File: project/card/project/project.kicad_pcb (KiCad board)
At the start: 2 copper layers, 29 parts, among them J1 USB_OTG, J2 Conn_01x06_Male, J3 Conn_01x02_Male, J5 Conn_Coaxial, J6 Conn_01x07_Female, J7 Conn_01x05_Female, SW1 SW_Push, SW2 SW_Push, U1 LM1117ADJ, U2 CMWX1ZZABZ-078

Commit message: layout etc
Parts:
- added C14: _, Capacitor_SMD:C_0805_2012Metric_Pad1.15x1.40mm_HandSolder, F.Cu at (94.8, 62.8)
- added C16: _, Capacitor_SMD:C_0805_2012Metric_Pad1.15x1.40mm_HandSolder, F.Cu at (95.7, 59.6)
- added D2: LED, LED_SMD:LED_0805_2012Metric_Pad1.15x1.40mm_HandSolder, F.Cu at (62.6, 72.5)
- added R4: 660, Resistor_SMD:R_0805_2012Metric_Pad1.15x1.40mm_HandSolder, F.Cu at (59.5, 72.5)
- added R5: 220, Resistor_SMD:R_0805_2012Metric_Pad1.15x1.40mm_HandSolder, F.Cu at (91.2, 52.5)
- C13: footprint Capacitor_SMD:CP_Elec_5x4.5 -> Capacitor_SMD:C_0805_2012Metric_Pad1.15x1.40mm_HandSolder
- J2: footprint Connector_Molex:Molex_KK-254_AE-6410-06A_1x06_P2.54mm_Vertical -> Connector_PinHeader_2.54mm:PinHeader_1x06_P2.54mm_Vertical
- J3: footprint Connector_Molex:Molex_KK-254_AE-6410-02A_1x02_P2.54mm_Vertical -> Connector_PinHeader_2.54mm:PinHeader_1x02_P2.54mm_Vertical
- J6: footprint Connector_Molex:Molex_KK-254_AE-6410-07A_1x07_P2.54mm_Vertical -> Connector_PinSocket_2.54mm:PinSocket_1x07_P2.54mm_Vertical
- J7: footprint Connector_Molex:Molex_KK-254_AE-6410-05A_1x05_P2.54mm_Vertical -> Connector_PinSocket_2.54mm:PinSocket_1x05_P2.54mm_Vertical
- U2: footprint RF_Module:CMWX1ZZABZ -> test:CMWX1ZZABZ
- moved C1 127.2 mm to (46.8, 56.1), turned to 180 degrees
- moved C7 126.3 mm to (48.6, 73.3), turned to 270 degrees
- moved J1 120.5 mm to (50.1, 38.8), turned to 180 degrees
- moved U1 118.8 mm to (52.0, 65.4), turned to 180 degrees
- moved C3 114.3 mm to (46.7, 52.2), turned to 180 degrees
- moved R3 113.7 mm to (61.5, 68.7)
- moved R2 111.1 mm to (60.6, 64.6), turned to 270 degrees
- moved C15 109.2 mm to (67.9, 60.2)
- moved C4 106.5 mm to (53.8, 54.4), turned to 270 degrees
- moved C11 103.1 mm to (68.1, 68.5)
- moved R1 101.0 mm to (75.9, 53.4), turned to 180 degrees
- moved C5 100.7 mm to (72.5, 60.2), turned to 180 degrees
- moved C8 100.0 mm to (55.5, 74.6), turned to 270 degrees
- moved C13 97.8 mm to (68.1, 64.1)
- moved C9 94.5 mm to (72.4, 68.6), turned to 180 degrees
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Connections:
- D1 pad 2: /LED -> Net-(D1-Pad2)
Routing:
- net +3V3: track 0.00 -> 146.8 mm, vias 0 -> 2
- net Net-(C2-Pad2): track 0.00 -> 38.2 mm
- net +5V: track 0.00 -> 33.1 mm
- net /DataCom: track 0.00 -> 32.0 mm, vias 0 -> 1
- net /Reset: track 0.00 -> 28.1 mm, vias 0 -> 2
- net /Piezo: track 0.00 -> 25.1 mm, vias 0 -> 2
- net Net-(J2-Pad2): track 0.00 -> 23.2 mm, vias 0 -> 1
- net /Btn: track 0.00 -> 21.7 mm, vias 0 -> 2
- net Net-(J2-Pad4): track 0.00 -> 21.4 mm, vias 0 -> 1
- net Net-(J6-Pad3): track 0.00 -> 19.4 mm
- net /echo: track 0.00 -> 17.4 mm, vias 0 -> 2
- net /trig: track 0.00 -> 16.1 mm
- net GND: track 0.00 -> 15.4 mm, vias 0 -> 2
- net Net-(C12-Pad2): track 0.00 -> 14.1 mm
- net Net-(J6-Pad4): track 0.00 -> 13.5 mm
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- added copper zone on B.Cu, net GND
- added copper zone on F.Cu, net GND
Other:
- net class Default: trace_width 0.25 -> 0.2
- net class Power added: clearance 0.2, trace_width 0.4, via_dia 0.8, via_drill 0.4

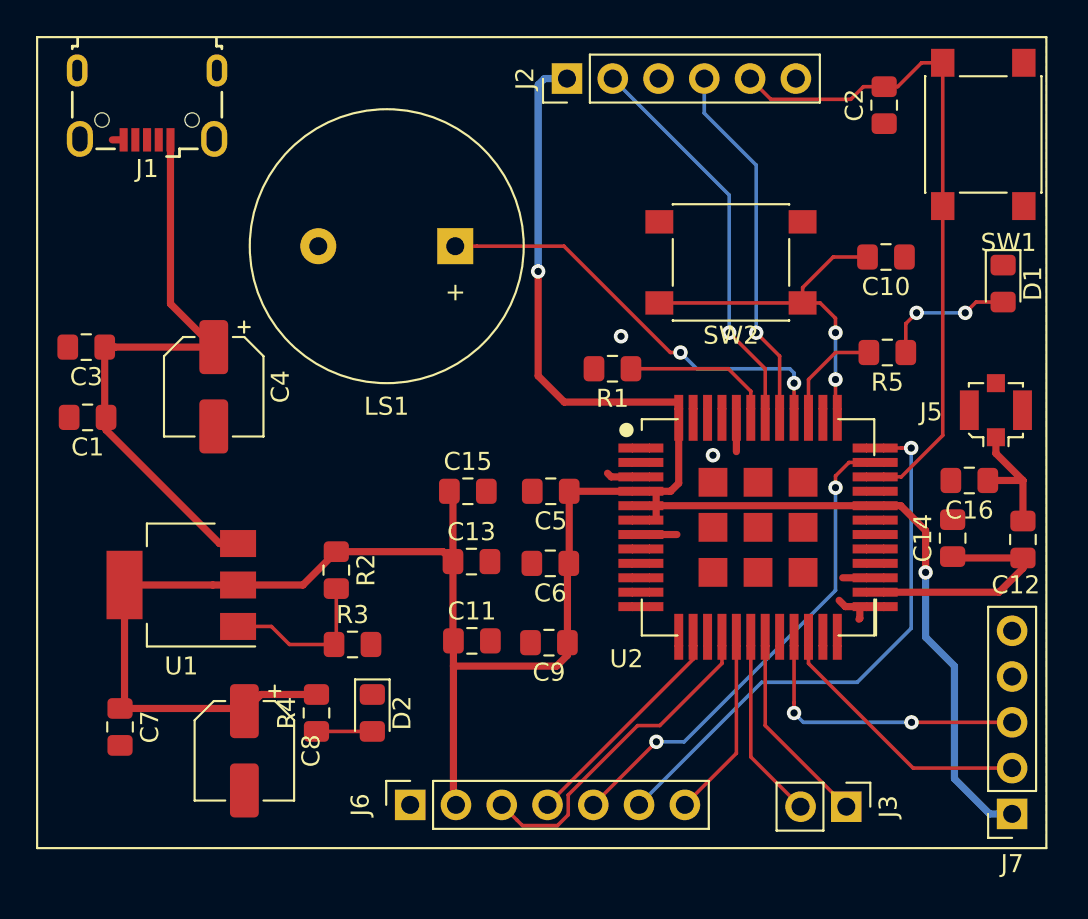
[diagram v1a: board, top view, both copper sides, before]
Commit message: fix routes and generate gerber
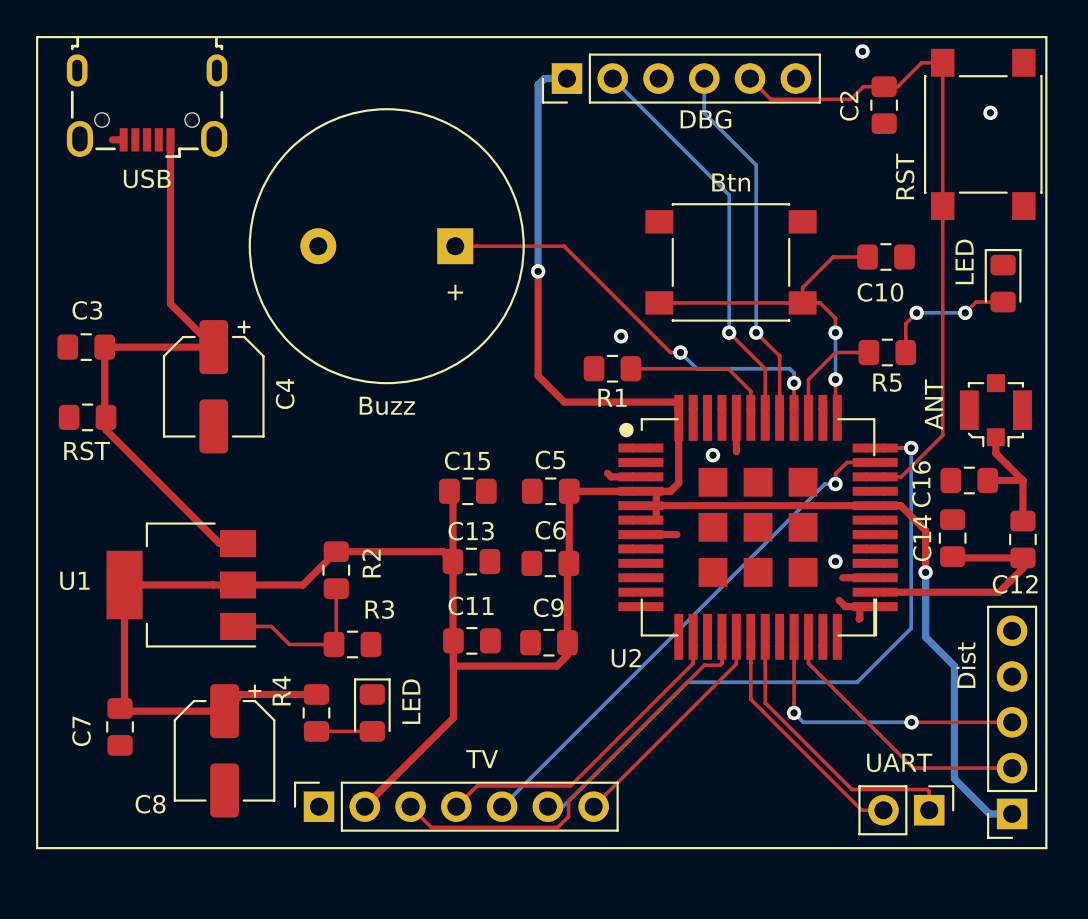
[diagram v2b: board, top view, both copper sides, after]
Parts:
- moved TV 5.06 mm to (59.6, 77.7)
- moved UART 4.60 mm to (93.5, 77.9)
- moved C8 1.10 mm to (54.4, 74.6)
- renumbered J5 to ANT, SW2 to Btn, LS1 to Buzz, J2 to DBG, J7 to Dist, D2 to LED, D1 to LED, SW1 to RST, C1 to RST, J6 to TV, J3 to UART, J1 to USB
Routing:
- net Net-(J6-Pad4): track 13.5 -> 18.8 mm
- net /DataCom: track 32.0 -> 37.1 mm
- net Net-(J6-Pad3): track 19.4 -> 24.4 mm
- net Net-(J3-Pad1): track 12.2 -> 16.7 mm
- net +3V3: track 146.8 -> 150.3 mm
- net Net-(J3-Pad2): track 11.4 -> 14.3 mm
- net /NSS: track 11.4 -> 13.6 mm
- net /Reset: track 28.1 -> 29.8 mm, vias 2 -> 1
- net GND: vias 2 -> 5
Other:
- net class Power: trace_width 0.4 -> 0.5
